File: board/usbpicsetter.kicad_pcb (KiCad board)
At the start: 2 copper layers, 37.3 x 18.2 mm, 10 parts, among them IC1 PIC10F200, P1 ICSP, Q1 PMOS

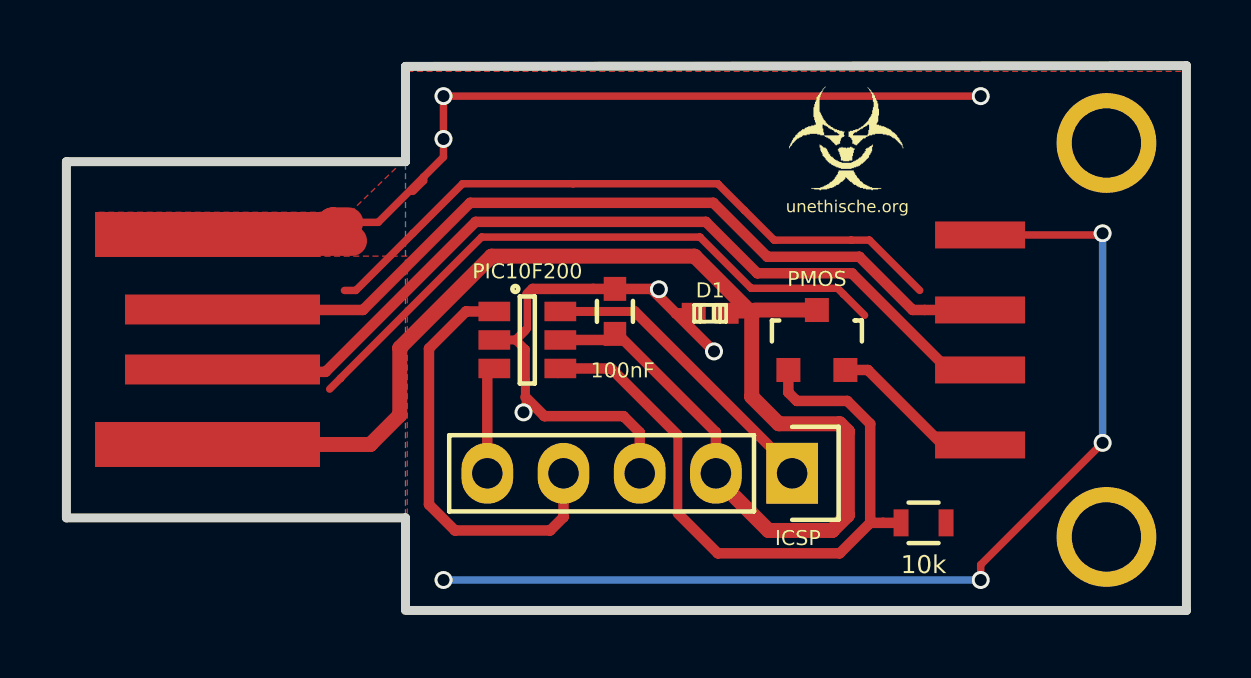
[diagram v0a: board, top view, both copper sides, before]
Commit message: Improved silk screen, generated gerbers and modified C programm
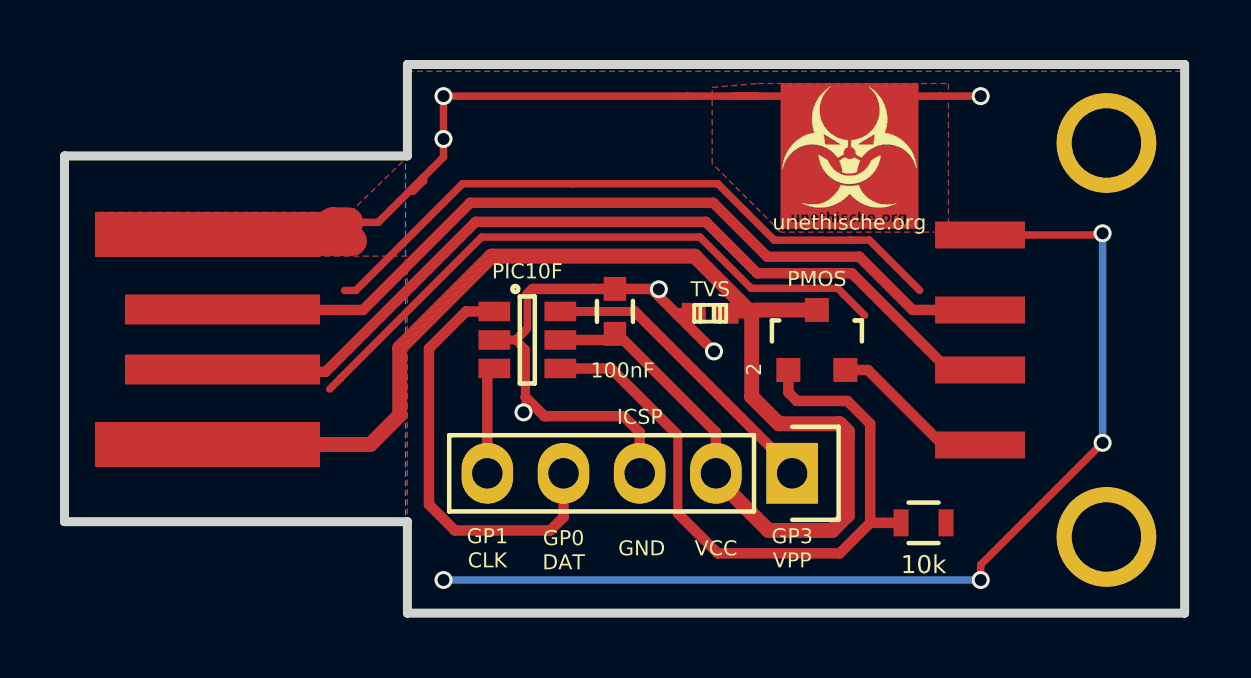
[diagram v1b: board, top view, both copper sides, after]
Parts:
- added G***: unethische.org, jcgb:unethi_silk, F.Cu at (97.3, 60.1)
- IC1: value PIC10F200 -> PIC10F
- O1: footprint jcgb:unethi_silk -> jcgb:unethi_copper_inv
- moved O1 2.41 mm to (97.3, 60.5)
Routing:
- net GND: track 89.6 -> 90.6 mm
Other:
- board size 37.3 x 18.2 mm -> 37.3 x 18.3 mm
- board text added: "2"
- board text added: "GND"
- board text added: "GP0 DAT"
- board text added: "GP1 CLK"
- board text added: "GP3 VPP"
- board text added: "VCC"

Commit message: Added labels
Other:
- board text added: "This board is optimized for home etching on a single sided board. The desing and code are public domain."
- board text added: "USB Resetter v0.3"
- board text removed: "This board is optimized for home etching on a single sided board. The desing and code is public domain."
- board text removed: "USB Resetter v0.2"
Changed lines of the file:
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@@
-(kicad_pcb (version 4) (host pcbnew 0.201509081510+6169~29~ubuntu14.04.1-product)
+(kicad_pcb (version 4) (host pcbnew 0.201510030350+6241~30~ubuntu14.04.1-product)
   (general
     (links 19)
     (no_connects 0)
-    (area 55.960287 49.607396 176.587859 113.525)
+    (area 70.969999 57.253999 108.608001 75.842001)
     (thickness 1.6)
-    (drawings 24)
+    (drawings 29)
     (tracks 152)
     (zones 0)
@@
     (title usbpicresetter)
     (date 2015-07-18)
-    (rev 0.2)
+    (rev 0.3)
     (company unethische.org)
   )
@@
     (visible_elements FFFFFF7F)
     (pcbplotparams
-      (layerselection 0x010f0_80000001)
-      (usegerberextensions false)
+      (layerselection 0x01030_80000001)
+      (usegerberextensions true)
       (excludeedgelayer true)
       (linewidth 0.100000)
@@
       (plotinvisibletext false)
       (padsonsilk false)
-      (subtractmaskfromsilk false)
-      (outputformat 4)
+      (subtractmaskfromsilk true)
+      (outputformat 1)
       (mirror false)
       (drillshape 0)
@@
       (xy -0.627077 -1.989906)) (layer F.SilkS) (width 0.01))
   )
+  (gr_text "GP3\nVPP" (at 95.377 73.533) (layer B.SilkS)
+    (effects (font (size 0.5 0.5) (thickness 0.1)) (justify mirror))
+  )
+  (gr_text VCC (at 92.837 73.533) (layer B.SilkS)
+    (effects (font (size 0.5 0.5) (thickness 0.1)) (justify mirror))
+  )
+  (gr_text GND (at 90.3605 73.533) (layer B.SilkS)
+    (effects (font (size 0.5 0.5) (thickness 0.1)) (justify mirror))
+  )
+  (gr_text "GP0\nDAT" (at 87.757 73.5965) (layer B.SilkS)
+    (effects (font (size 0.5 0.5) (thickness 0.1)) (justify mirror))
+  )
+  (gr_text "GP1\nCLK\n" (at 85.217 73.533) (layer F.SilkS)
+    (effects (font (size 0.5 0.5) (thickness 0.1)))
+  )
   (gr_text VCC (at 92.837 73.533) (layer F.SilkS)
     (effects (font (size 0.5 0.5) (thickness 0.1)))
@@
     (effects (font (size 0.5 0.5) (thickness 0.1)))
   )
-  (gr_text "GP1\nCLK\n" (at 85.217 73.533) (layer F.SilkS)
-    (effects (font (size 0.5 0.5) (thickness 0.1)))
+  (gr_text "GP1\nCLK\n" (at 85.217 73.533) (layer B.SilkS)
+    (effects (font (size 0.5 0.5) (thickness 0.1)) (justify mirror))
   )
   (gr_text "GP0\nDAT" (at 87.757 73.5965) (layer F.SilkS)
@@
   (gr_line (start 82.55 60.452) (end 82.55 57.404) (angle 90) (layer Edge.Cuts) (width 0.3))
   (gr_line (start 71.12 60.452) (end 82.55 60.452) (angle 90) (layer Edge.Cuts) (width 0.3))
-  (gr_text "This board is optimized for home etching on a single sided board.\nThe desing and code is public domain." (at 137.795 111.125) (layer Dwgs.User)
+  (gr_text "This board is optimized for home etching on a single sided board.\nThe desing and code are\n public domain." (at 137.795 111.125) (layer Dwgs.User)
     (effects (font (size 1.5 1.5) (thickness 0.3)))
   )
   (gr_line (start 92.770197 65.443277) (end 92.770197 65.951277) (layer F.SilkS) (width 0.15))
-  (gr_text "USB Resetter v0.2" (at 89.595197 59.791777) (layer F.Mask)
+  (gr_text "USB Resetter v0.3" (at 89.595197 59.791777) (layer F.Mask)
     (effects (font (size 0.8 0.7) (thickness 0.175)))
   )
